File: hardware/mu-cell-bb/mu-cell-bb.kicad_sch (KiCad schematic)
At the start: 74 parts, among them IC1 SX1255IWLTRT, J1 TX, J2 RX, J3 EXT_CLK, J4 RPi GPIO, J5 IO, Q1 BC817-40W, Q2 BC817-40W, U1 24LC256, U2 LDK130M33R, Y1 32MHz

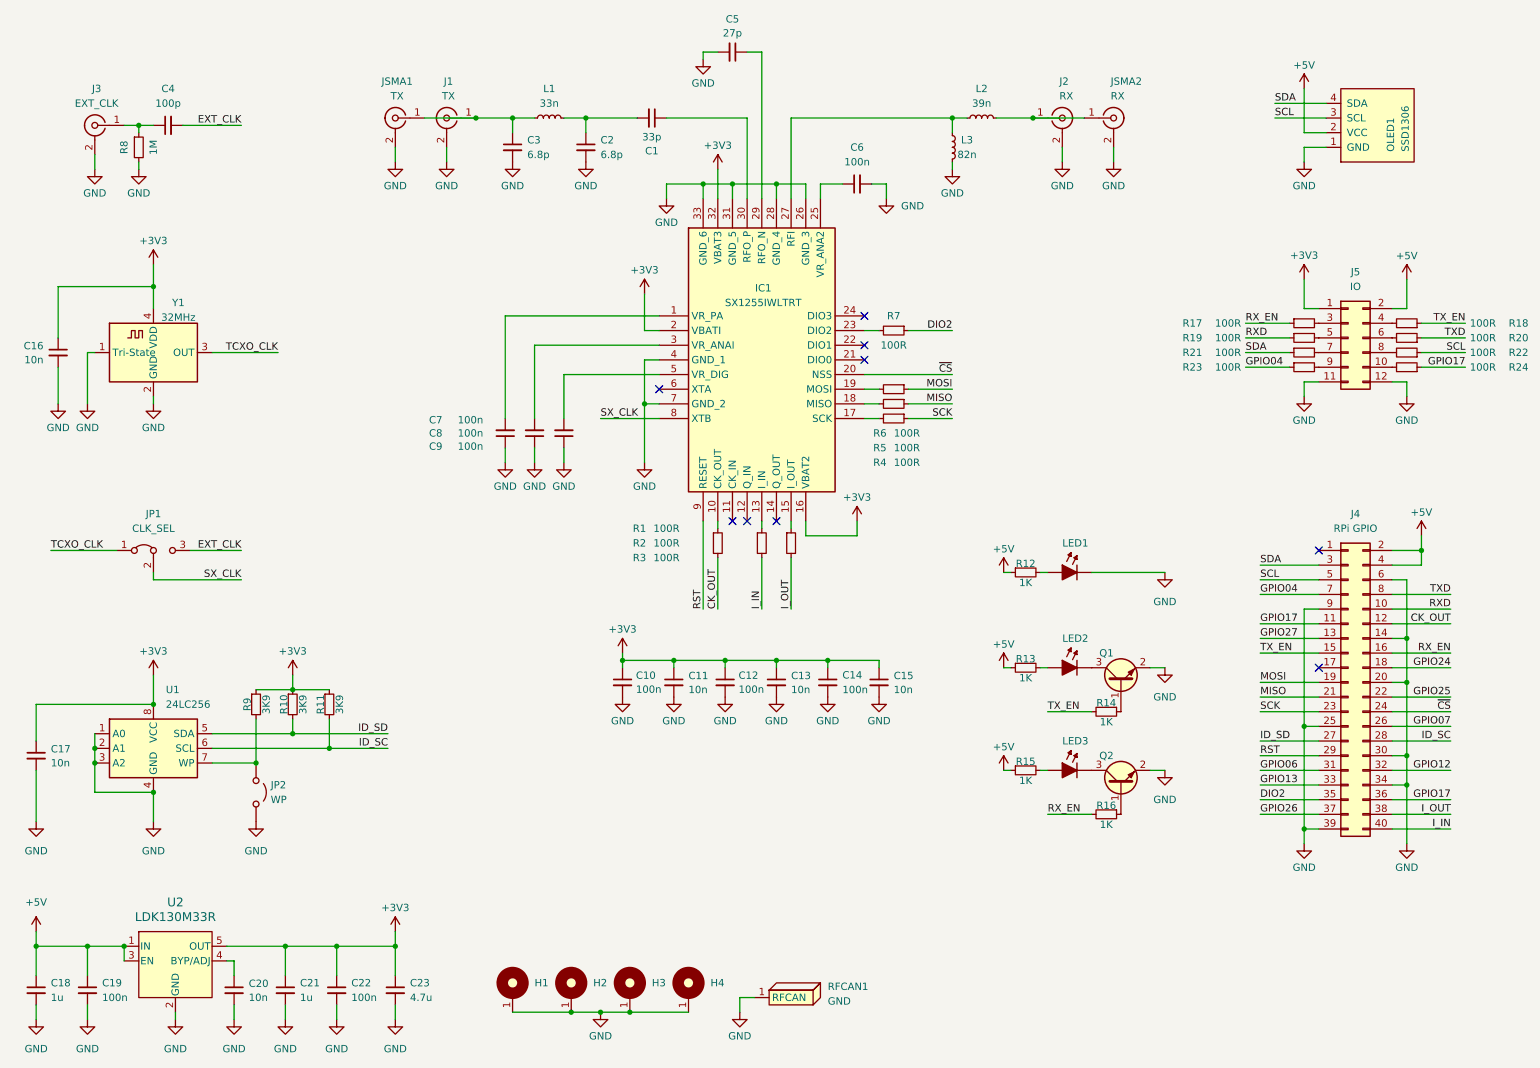
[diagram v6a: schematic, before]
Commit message: Routed majority of components
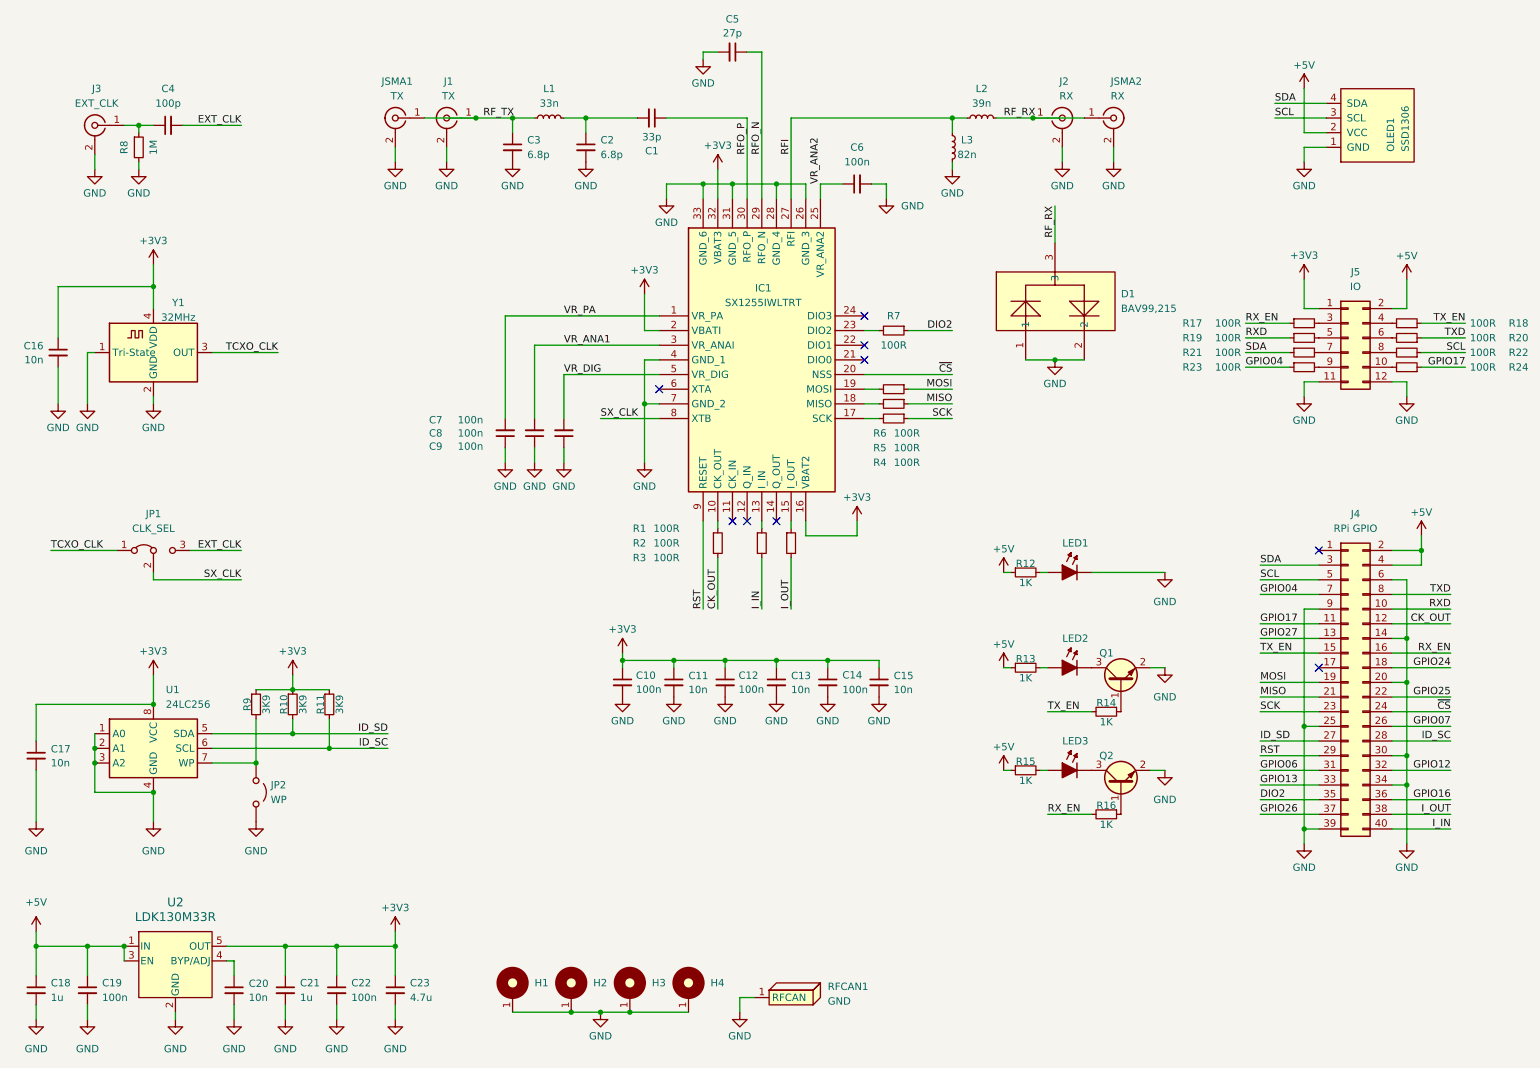
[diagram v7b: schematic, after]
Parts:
- added D1: BAV99,215, Package_TO_SOT_SMD:SOT-23-3, symbol parts:BAV99,215
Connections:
- net GND: now also D1.1, D1.2
- net GPIO17: no longer J4.36 (Pin_36)
- net RF_RX: now reaches J2.1 (In), JSMA2.1 (In), L2.1
- net RF_RX: now also D1.3
- net VR_PA: now reaches C7.2, IC1.1 (VR_PA)
- net RF_TX: now reaches C3.1, J1.1 (In), JSMA1.1 (In), L1.2
- net RFI: now reaches IC1.27 (RFI), L2.2, L3.2
- net VR_ANA1: now reaches C8.2, IC1.3 (VR_ANAI)
- net VR_ANA2: now reaches C6.1, IC1.25 (VR_ANA2)
- net RFO_N: now reaches C5.1, IC1.29 (RFO_N)
- net RFO_P: now reaches C1.1, IC1.30 (RFO_P)
- net VR_DIG: now reaches C9.2, IC1.5 (VR_DIG)
- new net GPIO16: J4.36 (Pin_36)

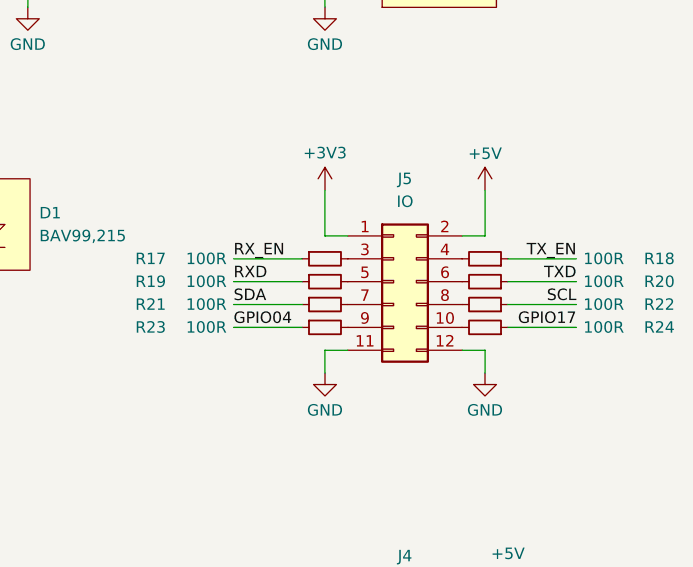
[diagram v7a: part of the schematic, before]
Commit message: added LCSC parts, finished routing
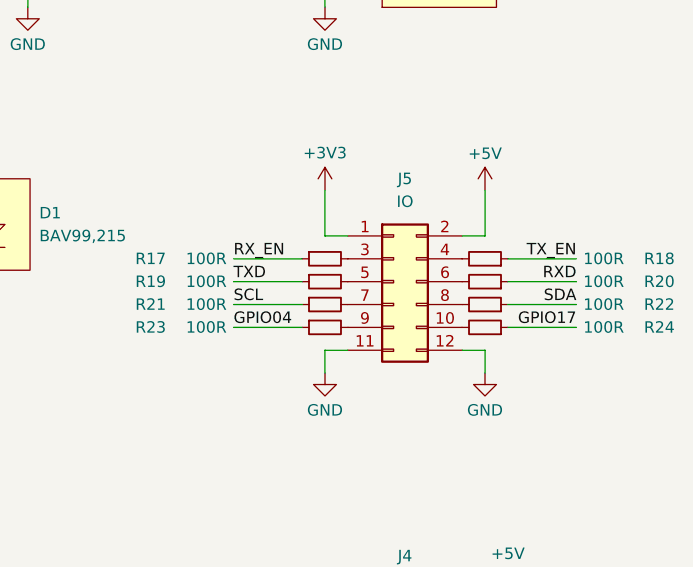
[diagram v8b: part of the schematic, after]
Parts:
- C1: LCSC Part (none) -> C437439; MPN VJ0603A330KXAPW1BC -> (none); PN 77-VJ0603A330KXAPBC -> (none)
- C10, C12, C14, C19, C22, C6, C7, C8, C9: LCSC Part (none) -> C60474; PN 581-06035G104Z -> (none)
- C11, C13, C15, C16, C17, C20: LCSC Part (none) -> C60133; PN 80-C0603C103M4RECLR -> (none)
- C18, C21: LCSC Part (none) -> C29266; PN 581-06035G104Z -> (none)
- C2, C3: LCSC Part (none) -> C1864373; MPN 06035G104ZAT2A -> (none); PN 581-06035G104Z -> (none)
- C23: LCSC Part (none) -> C23733; PN 581-06035G104Z -> (none)
- C4: LCSC Part (none) -> C2941926; PN 581-06035G104Z -> (none)
- C5: LCSC Part (none) -> C3889037; PN 603-AC0603JRNP9BN270 -> (none)
- H1, H2, H3, H4, J5, JP2, JSMA1, JSMA2, OLED1: now left out of the parts list
- IC1: LCSC Part (none) -> C89372
- J1, J2, J3: LCSC Part (none) -> C5137195
- L1: LCSC Part (none) -> C39885562; PN 815-AISC-0603-R039-J -> (none)
- L2: LCSC Part (none) -> C40399699; PN 815-AISC-0603-R039-J -> (none)
- L3: LCSC Part (none) -> C38907014; PN 815-AISC-0603-R082-J -> (none)
- LED1: value LED_0603 -> Green
- LED2: value LED_0603 -> Red
- LED3: value LED_0603 -> Yellow
- Q1, Q2: LCSC Part (none) -> C383187
- R1, R17, R18, R19, R2, R20, R21, R22, R23, R24, R3, R4, R5, R6, R7: LCSC Part (none) -> C106232; PN CRCW0603100RFKECC -> (none)
- R10, R11, R9: LCSC Part (none) -> C2909346; PN CRCW06033K9FKECC -> (none)
- R12, R13, R14, R15, R16: LCSC Part (none) -> C106235; PN CRCW06033K9FKECC -> (none)
- R8: LCSC Part (none) -> C26083; PN CRCW0603100RFKECC -> (none)
- RFCAN1: LCSC Part (none) -> C22418535
- U1: LCSC Part (none) -> C615210
- U2: LCSC Part (none) -> C2969807
- Y1: LCSC Part (none) -> C48332760
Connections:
- net RXD: now also R20.1; no longer R19.1
- net SCL: now also R21.1; no longer R22.1
- net SDA: now also R22.1; no longer R21.1
- net TXD: now also R19.1; no longer R20.1
